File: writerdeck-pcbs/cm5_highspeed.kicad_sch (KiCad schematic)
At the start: 1 part

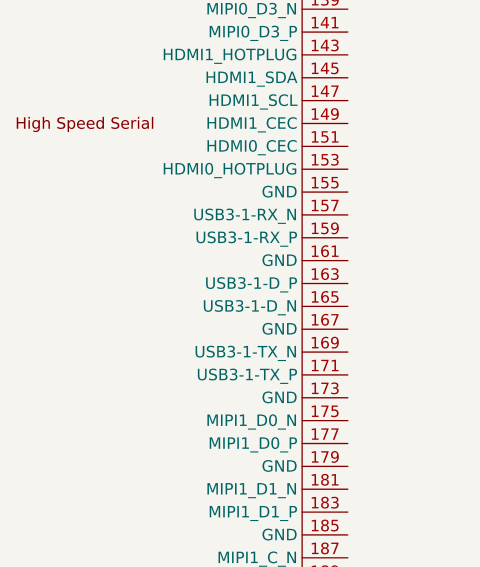
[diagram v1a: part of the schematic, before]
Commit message: pre switch matrix, restructure
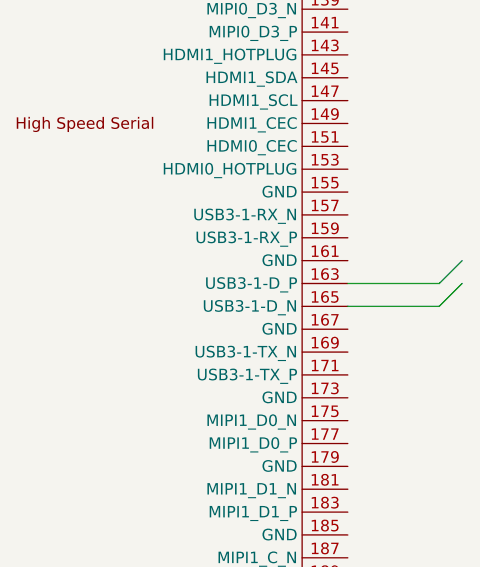
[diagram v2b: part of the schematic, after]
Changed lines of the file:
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@@
 	(generator_version "9.0")
 	(paper "A4")
+	(bus_entry
+		(at 106.68 115.57)
+		(size 2.54 -2.54)
+		(stroke
+			(width 0)
+			(type default)
+		)
+	)
+	(bus_entry
+		(at 106.68 118.11)
+		(size 2.54 -2.54)
+		(stroke
+			(width 0)
+			(type default)
+		)
+	)
+	(wire
+		(pts
+			(xy 96.52 115.57) (xy 106.68 115.57)
+		)
+		(stroke
+			(width 0)
+			(type default)
+		)
+	)
+	(wire
+		(pts
+			(xy 96.52 118.11) (xy 106.68 118.11)
+		)
+		(stroke
+			(width 0)
+			(type default)
+		)
+	)
 	(symbol
 		(lib_id "ZF_common:ComputeModule5-CM5")
@@
 		)
 		(instances
-			(project ""
-				(path "/61242ec3-a4bb-4627-ba23-da2822f5a571/bce3ac00-aa35-4f10-a603-8a5cc904f72f/59a7a95d-8086-4b83-a4eb-11bfc5b8db86"
+			(project "writerdeck-pcbs"
+				(path "/61242ec3-a4bb-4627-ba23-da2822f5a571/cfede3bf-c957-4dc1-890c-2e9bdf4e2ec0"
 					(reference "Module1")
 					(unit 2)

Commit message: backup
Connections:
- net USB2_P: now reaches Module1.134 (USB3-0-D_P)
- net USB2_N: now reaches Module1.136 (USB3-0-D_N)
- no-connect marks 0 -> 33
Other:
- moved on the sheet: Module1B
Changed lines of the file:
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@@
 	(generator_version "9.0")
 	(paper "A4")
+	(no_connect
+		(at 36.83 62.23)
+	)
+	(no_connect
+		(at 97.79 102.87)
+	)
+	(no_connect
+		(at 36.83 115.57)
+	)
+	(no_connect
+		(at 36.83 100.33)
+	)
+	(no_connect
+		(at 36.83 92.71)
+	)
+	(no_connect
+		(at 36.83 110.49)
+	)
+	(no_connect
+		(at 36.83 133.35)
+	)
+	(no_connect
+		(at 36.83 130.81)
+	)
+	(no_connect
+		(at 97.79 97.79)
+	)
+	(no_connect
+		(at 36.83 46.99)
+	)
+	(no_connect
+		(at 97.79 92.71)
+	)
+	(no_connect
+		(at 36.83 64.77)
+	)
+	(no_connect
+		(at 36.83 95.25)
+	)
+	(no_connect
+		(at 97.79 95.25)
+	)
+	(no_connect
+		(at 97.79 161.29)
+	)
+	(no_connect
+		(at 36.83 54.61)
+	)
+	(no_connect
+		(at 36.83 138.43)
+	)
+	(no_connect
+		(at 36.83 41.91)
+	)
+	(no_connect
+		(at 97.79 90.17)
+	)
+	(no_connect
+		(at 36.83 148.59)
+	)
+	(no_connect
+		(at 97.79 100.33)
+	)
+	(no_connect
+		(at 36.83 39.37)
+	)
+	(no_connect
+		(at 36.83 57.15)
+	)
+	(no_connect
+		(at 36.83 118.11)
+	)
+	(no_connect
+		(at 36.83 146.05)
+	)
+	(no_connect
+		(at 36.83 123.19)
+	)
+	(no_connect
+		(at 36.83 140.97)
+	)
+	(no_connect
+		(at 36.83 102.87)
+	)
+	(no_connect
+		(at 36.83 125.73)
+	)
+	(no_connect
+		(at 36.83 161.29)
+	)
+	(no_connect
+		(at 36.83 107.95)
+	)
+	(no_connect
+		(at 36.83 49.53)
+	)
+	(no_connect
+		(at 36.83 36.83)
+	)
 	(bus_entry
-		(at 106.68 115.57)
-		(size 2.54 -2.54)
+		(at 25.4 74.93)
+		(size 2.54 2.54)
 		(stroke
 			(width 0)
@@
 	)
 	(bus_entry
-		(at 106.68 118.11)
-		(size 2.54 -2.54)
+		(at 25.4 77.47)
+		(size 2.54 2.54)
 		(stroke
 			(width 0)
@@
 	(wire
 		(pts
-			(xy 96.52 115.57) (xy 106.68 115.57)
+			(xy 27.94 80.01) (xy 36.83 80.01)
 		)
 		(stroke
@@
 	(wire
 		(pts
-			(xy 96.52 118.11) (xy 106.68 118.11)
-		)
-		(stroke
-			(width 0)
-			(type default)
+			(xy 27.94 77.47) (xy 36.83 77.47)
+		)
+		(stroke
+			(width 0)
+			(type default)
+		)
+	)
+	(bus
+		(pts
+			(xy 25.4 72.39) (xy 25.4 74.93)
+		)
+		(stroke
+			(width 0)
+			(type default)
+		)
+	)
+	(bus
+		(pts
+			(xy 25.4 74.93) (xy 25.4 77.47)
+		)
+		(stroke
+			(width 0)
+			(type default)
+		)
+	)
+	(label "USB2_N"
+		(at 27.94 80.01 0)
+		(effects
+			(font
+				(size 1.27 1.27)
+			)
+			(justify left bottom)
+		)
+	)
+	(label "USB2_P"
+		(at 27.94 77.47 0)
+		(effects
+			(font
+				(size 1.27 1.27)
+			)
+			(justify left bottom)
+		)
+	)
+	(hierarchical_label "{USB2}"
+		(shape bidirectional)
+		(at 25.4 72.39 180)
+		(effects
+			(font
+				(size 1.27 1.27)
+			)
+			(justify right)
+		)
+	)
+	(hierarchical_label "{USB3}"
+		(shape bidirectional)
+		(at 24.13 59.69 180)
+		(effects
+			(font
+				(size 1.27 1.27)
+			)
+			(justify right)
 		)
 	)
 	(symbol
 		(lib_id "ZF_common:ComputeModule5-CM5")
-		(at -73.66 97.79 0)
+		(at -72.39 97.79 0)
 		(unit 2)
 		(exclude_from_sim no)
@@
 		(fields_autoplaced yes)
 		(property "Reference" "Module1"
-			(at 66.04 24.13 0)
+			(at 67.31 24.13 0)
 			(effects
 				(font
@@
 		)
 		(property "Value" "ComputeModule5-CM5"
-			(at 66.04 26.67 0)
+			(at 67.31 26.67 0)
 			(effects
 				(font
@@
 		)
 		(property "Footprint" "ZF_common:Raspberry-Pi-5-Compute-Module"
-			(at 68.58 124.46 0)
+			(at 69.85 124.46 0)
 			(effects
 				(font
@@
 		)
 		(property "Datasheet" "https://pip-assets.raspberrypi.com/categories/944-raspberry-pi-compute-module-5/documents/RP-008180-DS-6-cm5-datasheet.pdf"
-			(at 68.58 124.46 0)
+			(at 69.85 124.46 0)
 			(effects
 				(font
@@
 		)
 		(property "Description" "RaspberryPi Compute module 5"
-			(at -73.66 97.79 0)
+			(at -72.39 97.79 0)
 			(effects
 				(font
@@
 		)
 		(property "Field4" "Amphenol"
-			(at 66.04 29.21 0)
+			(at 67.31 29.21 0)
 			(effects
 				(font
@@
 		)
 		(property "Field5" "2x 10164227-1001A1RLF"
-			(at 66.04 31.75 0)
-			(effects
-				(font
+			(at 67.31 31.75 0)
+			(effects
+				(font
